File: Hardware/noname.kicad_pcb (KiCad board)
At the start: 2 copper layers, 57.1 x 50.2 mm, 37 parts, among them P1 VIN, P10 UART, P11 AREF, P12 Mounting Hole, P13 Mounting Hole, P14 Mounting Hole, P15 Mounting Hole, P2 PORTB, P3 PORTC, P4 PORTD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

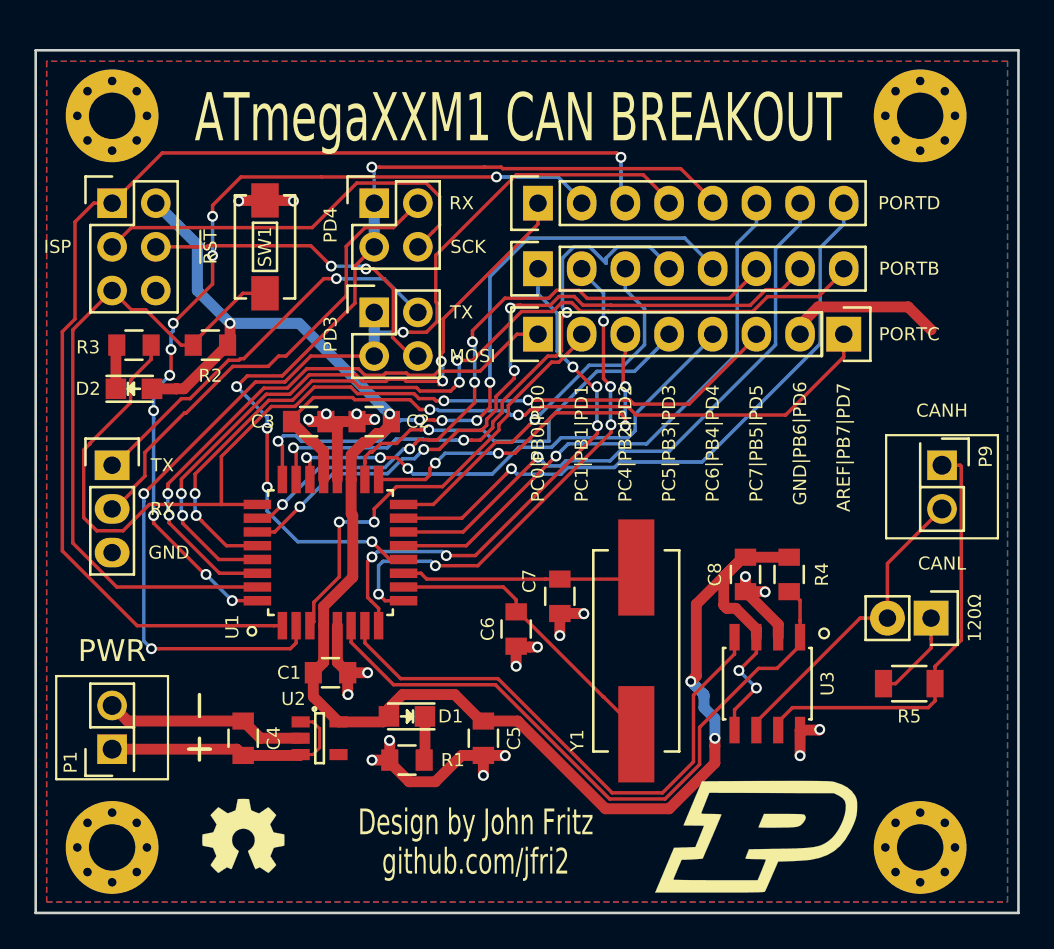
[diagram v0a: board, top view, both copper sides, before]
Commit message: Cleaned up PCB, added silkscreen & logos
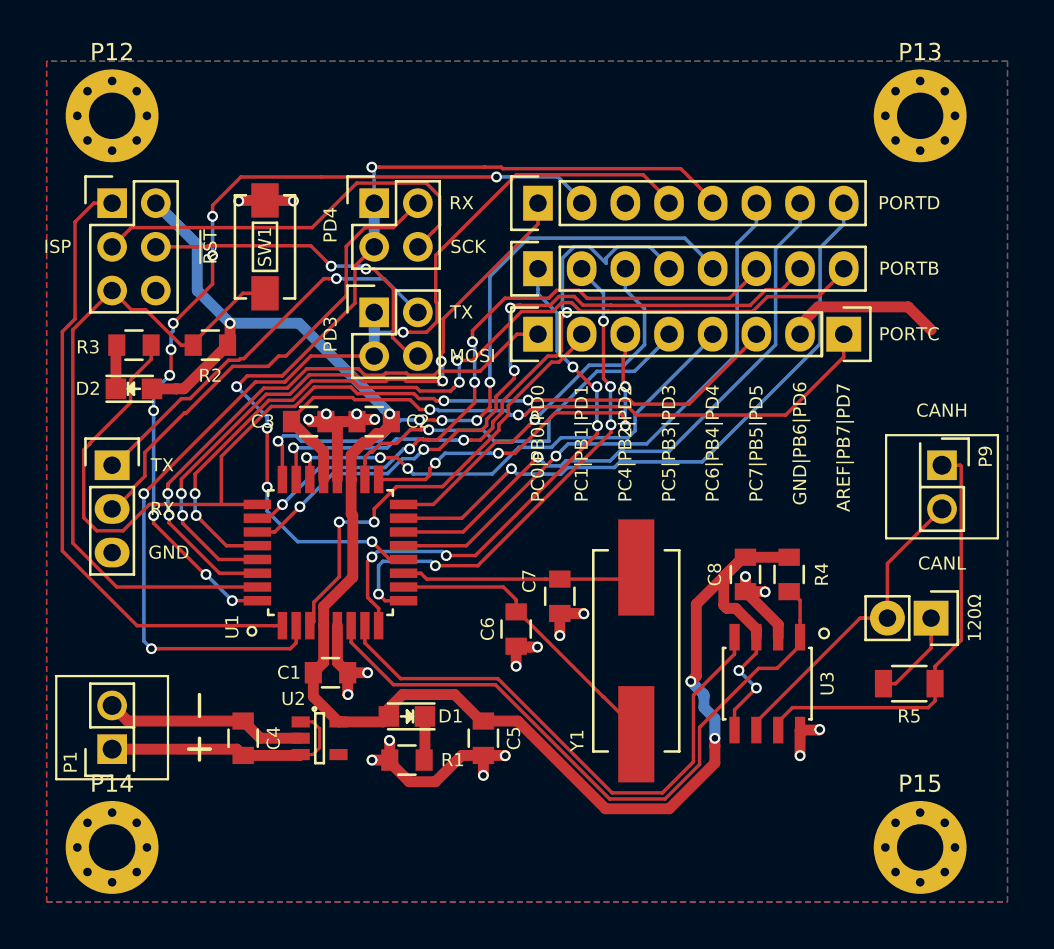
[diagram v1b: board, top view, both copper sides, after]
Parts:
- removed G***: LOGO, Graphics:oshw
- removed G***: LOGO, Graphics:purdue
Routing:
- net AVR_MISO: track 70.3 -> 36.6 mm, vias 1 -> 0
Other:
- board outline removed
- board text removed: "ATmegaXXM1 CAN BREAKOUT"
- board text removed: "Design by John Fritz"
- board text removed: "PWR"
- board text removed: "github.com/jfri2"
